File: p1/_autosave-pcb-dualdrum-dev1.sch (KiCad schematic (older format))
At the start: 154 parts, among them P1 CONN-02x05, U1 082, U2 082, U3 082, U4 082, U5 082, U6 082, U7 082, U8 082-NJM, U9 082

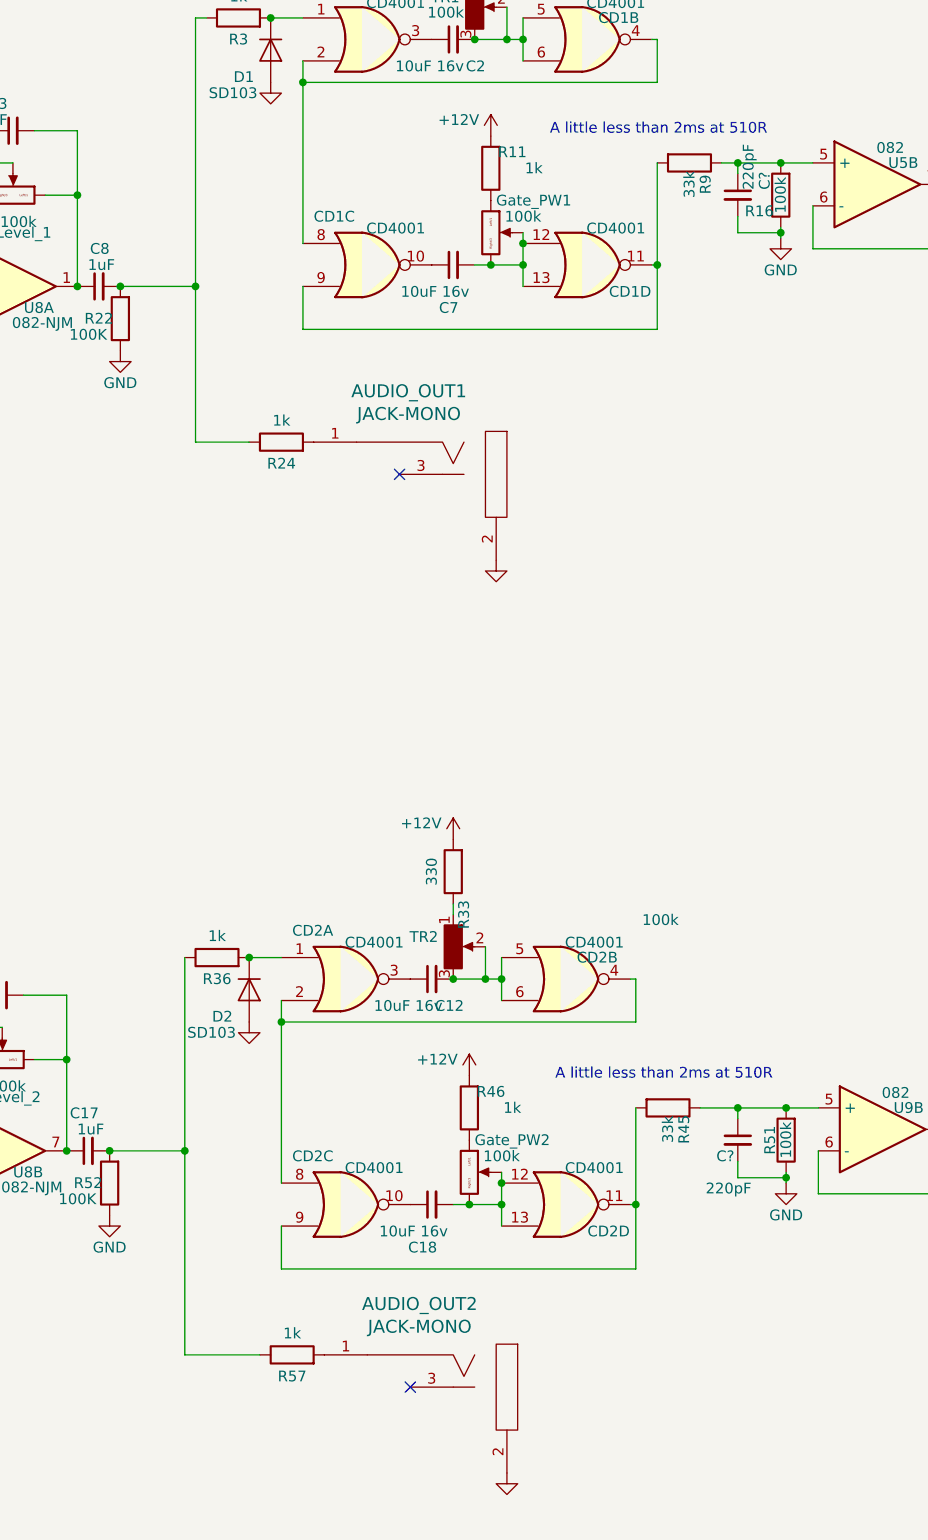
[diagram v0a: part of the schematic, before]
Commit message: beginning to lay tracks
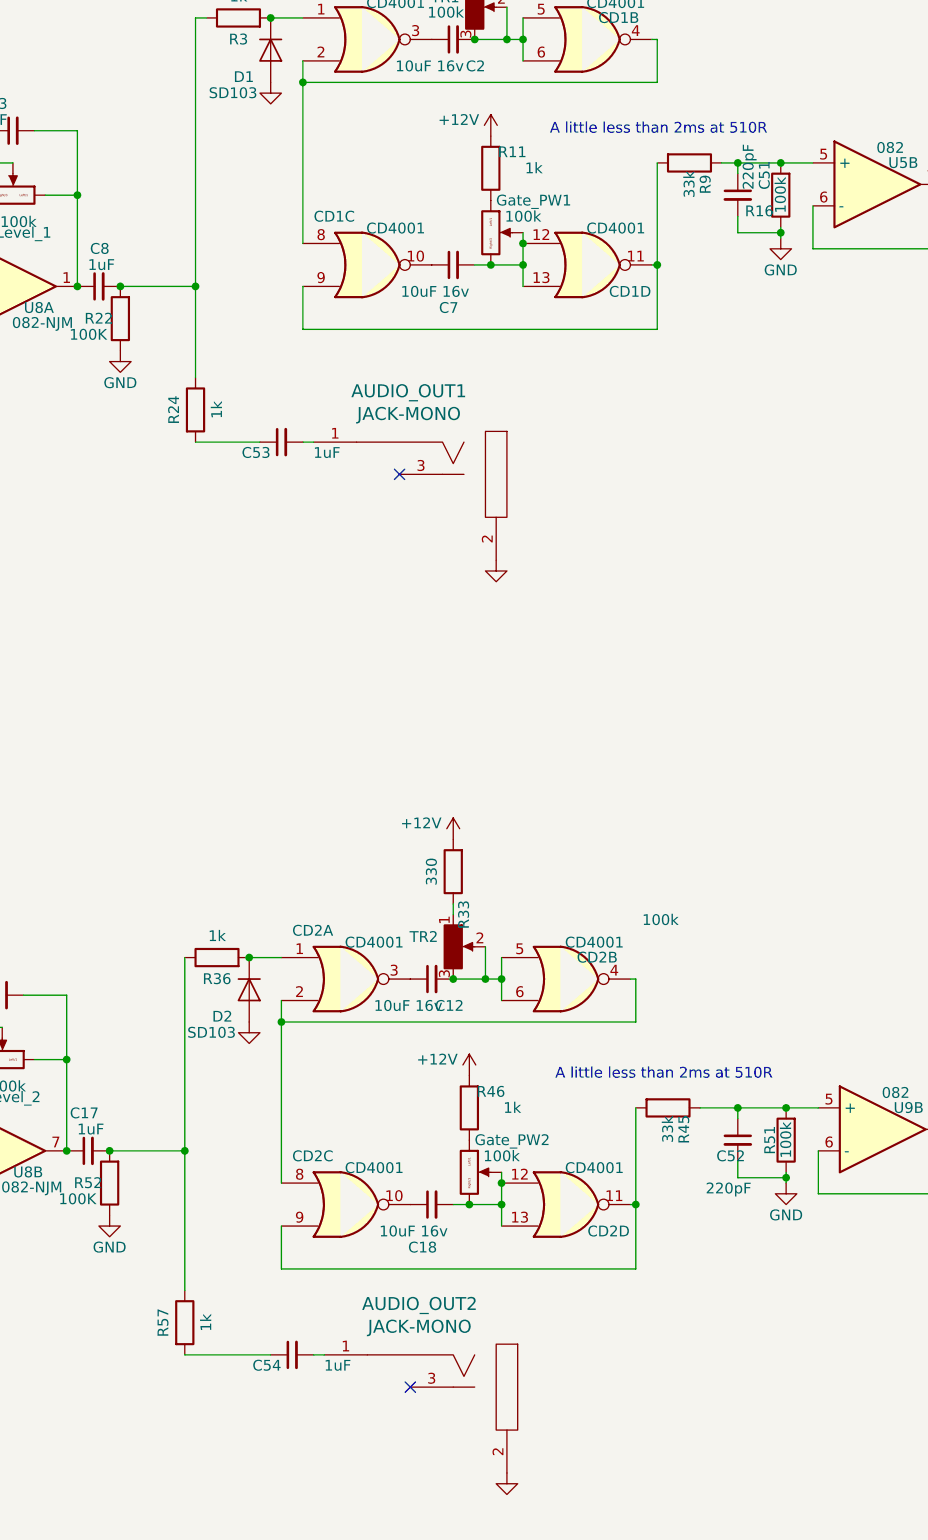
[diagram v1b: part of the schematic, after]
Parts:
- added C53, C54: 1uF, 4ms_Capacitor:C_0603, symbol 4ms-passives:C_Small
- gave numbers to parts that had none: 2
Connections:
- wire segments 348 -> 350
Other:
- moved on the sheet: R24, R57
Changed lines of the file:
@@
 L 4ms-passives:R R?
 U 1 1 5D7B1AC0
-P 11575 3250
+P 11175 3100
 AR Path="/5B8C674E/5D7B1AC0" Ref="R?"  Part="1"
 AR Path="/5D7B1AC0" Ref="R24"  Part="1"
 AR Path="/5E7668A3/5D7B1AC0" Ref="R?"  Part="1"
-F 0 "R24" V 11475 3250 50  0000 C CNN
-F 1 "1k" V 11675 3250 50  0000 C CNN
-F 2 "4ms_Resistor:R_0603" H 11575 3250 60  0001 C CNN
-F 3 "" H 11575 3250 60  0000 C CNN
-F 4 "Mouser" H 5975 1450 50  0001 C CNN "Manufacturer"
-F 5 "Substitution OK" H 5975 1450 50  0001 C CNN "Comments"
-F 6 "1%,1/10W,0603" H 5975 1450 50  0001 C CNN "Designation"
-F 7 "RC0603FR-07XXXL" H 5975 1450 50  0001 C CNN "Part Number"
-F 8 "C0603" H 5975 1450 50  0001 C CNN "Package"
-	1    11575 3250
-	0    -1   -1   0
+F 0 "R24" V 11075 3100 50  0000 C CNN
+F 1 "1k" V 11275 3100 50  0000 C CNN
+F 2 "4ms_Resistor:R_0603" H 11175 3100 60  0001 C CNN
+F 3 "" H 11175 3100 60  0000 C CNN
+F 4 "Mouser" H 5575 1300 50  0001 C CNN "Manufacturer"
+F 5 "Substitution OK" H 5575 1300 50  0001 C CNN "Comments"
+F 6 "1%,1/10W,0603" H 5575 1300 50  0001 C CNN "Designation"
+F 7 "RC0603FR-07XXXL" H 5575 1300 50  0001 C CNN "Part Number"
+F 8 "C0603" H 5575 1300 50  0001 C CNN "Package"
+	1    11175 3100
+	1    0    0    -1
 $EndComp
 $Comp
@@
 $EndComp
 Wire Wire Line
-	11175 2525 11175 3250
-Wire Wire Line
-	11175 3250 11425 3250
-Connection ~ 11175 2525
-Wire Wire Line
 	11175 1275 11225 1275
 Wire Wire Line
@@
 L 4ms-passives:R R?
 U 1 1 5D83757F
-P 11625 7500
+P 11125 7350
 AR Path="/5B8C674E/5D83757F" Ref="R?"  Part="1"
 AR Path="/5D83757F" Ref="R57"  Part="1"
 AR Path="/5E7668A3/5D83757F" Ref="R?"  Part="1"
-F 0 "R57" V 11525 7500 50  0000 C CNN
-F 1 "1k" V 11725 7500 50  0000 C CNN
-F 2 "4ms_Resistor:R_0603" H 11625 7500 60  0001 C CNN
-F 3 "" H 11625 7500 60  0000 C CNN
-F 4 "Mouser" H 6025 5700 50  0001 C CNN "Manufacturer"
-F 5 "Substitution OK" H 6025 5700 50  0001 C CNN "Comments"
-F 6 "1%,1/10W,0603" H 6025 5700 50  0001 C CNN "Designation"
-F 7 "RC0603FR-07XXXL" H 6025 5700 50  0001 C CNN "Part Number"
-F 8 "C0603" H 6025 5700 50  0001 C CNN "Package"
-	1    11625 7500
-	0    -1   -1   0
+F 0 "R57" V 11025 7350 50  0000 C CNN
+F 1 "1k" V 11225 7350 50  0000 C CNN
+F 2 "4ms_Resistor:R_0603" H 11125 7350 60  0001 C CNN
+F 3 "" H 11125 7350 60  0000 C CNN
+F 4 "Mouser" H 5525 5550 50  0001 C CNN "Manufacturer"
+F 5 "Substitution OK" H 5525 5550 50  0001 C CNN "Comments"
+F 6 "1%,1/10W,0603" H 5525 5550 50  0001 C CNN "Designation"
+F 7 "RC0603FR-07XXXL" H 5525 5550 50  0001 C CNN "Part Number"
+F 8 "C0603" H 5525 5550 50  0001 C CNN "Package"
+	1    11125 7350
+	1    0    0    -1
 $EndComp
 $Comp
@@
 Wire Wire Line
 	11125 5650 11125 6550
-Wire Wire Line
-	11475 7500 11125 7500
-Wire Wire Line
-	11125 7500 11125 6550
-Connection ~ 11125 6550
 $Comp
 L 4ms-headers:Conn_01x03 Bypass_2nd_Filter1
@@
 P 13700 2100
 AR Path="/5B8C674E/5D770733" Ref="C?"  Part="1"
-AR Path="/5D770733" Ref="C?"  Part="1"
+AR Path="/5D770733" Ref="C51"  Part="1"
 AR Path="/5E7668A3/5D770733" Ref="C?"  Part="1"
-F 0 "C?" V 13825 2125 50  0000 L CNN
+F 0 "C51" V 13825 2125 50  0000 L CNN
 F 1 "220pF" V 13750 2125 50  0000 L CNN
 F 2 "4ms_Capacitor:C_0603" H 13700 2100 50  0001 C CNN
@@
 P 13700 6500
 AR Path="/5B8C674E/5D834A5A" Ref="C?"  Part="1"
-AR Path="/5D834A5A" Ref="C?"  Part="1"
+AR Path="/5D834A5A" Ref="C52"  Part="1"
 AR Path="/5E7668A3/5D834A5A" Ref="C?"  Part="1"
-F 0 "C?" H 13600 6425 50  0000 L CNN
+F 0 "C52" H 13600 6425 50  0000 L CNN
 F 1 "220pF" H 13550 6275 50  0000 L CNN
 F 2 "4ms_Capacitor:C_0603" H 13700 6500 50  0001 C CNN
@@
 	13925 6700 13925 6675
 Connection ~ 13925 6675
+$Comp
+L 4ms-passives:C_Small C?
+U 1 1 5D9AD2ED
+P 11575 3250
+AR Path="/5B8C674E/5D9AD2ED" Ref="C?"  Part="1"
+AR Path="/5D9AD2ED" Ref="C53"  Part="1"
+AR Path="/5E7668A3/5D9AD2ED" Ref="C?"  Part="1"
+F 0 "C53" V 11525 3300 50  0000 L CNN
+F 1 "1uF" V 11525 2975 50  0000 L CNN
+F 2 "4ms_Capacitor:C_0603" H 11575 3250 50  0001 C CNN
+F 3 "" H 11575 3250 50  0000 C CNN
+F 4 "Mouser" H 7425 1450 50  0001 C CNN "Manufacturer"
+F 5 "Substitution OK" H 7425 1450 50  0001 C CNN "Comments"
+F 6 "16V,10%,X5R or X7R,0603" H 7425 1450 50  0001 C CNN "Designation"
+F 7 "C0603" H 7425 1450 50  0001 C CNN "Package"
+F 8 "TEST" H 7425 1450 50  0001 C CNN "Part Number"
+F 9 "2" H 7425 1450 50  0001 C CNN "Points"
+F 10 "SMD" H 7425 1450 50  0001 C CNN "SMD/TH"
+	1    11575 3250
+	0    -1   -1   0
+$EndComp
+Wire Wire Line
+	11175 2525 11175 2950
+Connection ~ 11175 2525
+Wire Wire Line
+	11175 3250 11475 3250
+Wire Wire Line
+	11675 3250 11725 3250
+$Comp
+L 4ms-passives:C_Small C?
+U 1 1 5DA4667F
+P 11625 7500
+AR Path="/5B8C674E/5DA4667F" Ref="C?"  Part="1"
+AR Path="/5DA4667F" Ref="C54"  Part="1"
+AR Path="/5E7668A3/5DA4667F" Ref="C?"  Part="1"
+F 0 "C54" V 11575 7550 50  0000 L CNN
+F 1 "1uF" V 11575 7225 50  0000 L CNN
+F 2 "4ms_Capacitor:C_0603" H 11625 7500 50  0001 C CNN
+F 3 "" H 11625 7500 50  0000 C CNN
+F 4 "Mouser" H 7475 5700 50  0001 C CNN "Manufacturer"
+F 5 "Substitution OK" H 7475 5700 50  0001 C CNN "Comments"
+F 6 "16V,10%,X5R or X7R,0603" H 7475 5700 50  0001 C CNN "Designation"
+F 7 "C0603" H 7475 5700 50  0001 C CNN "Package"
+F 8 "TEST" H 7475 5700 50  0001 C CNN "Part Number"
+F 9 "2" H 7475 5700 50  0001 C CNN "Points"
+F 10 "SMD" H 7475 5700 50  0001 C CNN "SMD/TH"
+	1    11625 7500
+	0    -1   -1   0
+$EndComp
+Wire Wire Line
+	11125 7500 11525 7500
+Wire Wire Line
+	11725 7500 11775 7500
+Wire Wire Line
+	11125 6550 11125 7200
+Connection ~ 11125 6550
 $EndSCHEMATC
